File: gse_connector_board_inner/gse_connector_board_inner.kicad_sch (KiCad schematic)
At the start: 26 parts, among them J1 arming_connector, J2 gse_com_connector, J3 chg_connector, J4 Conn_02x03_Top_Bottom, J5 Conn_02x02_Top_Bottom, U7 ISO1044BD, U9 MCP2562-E-SN

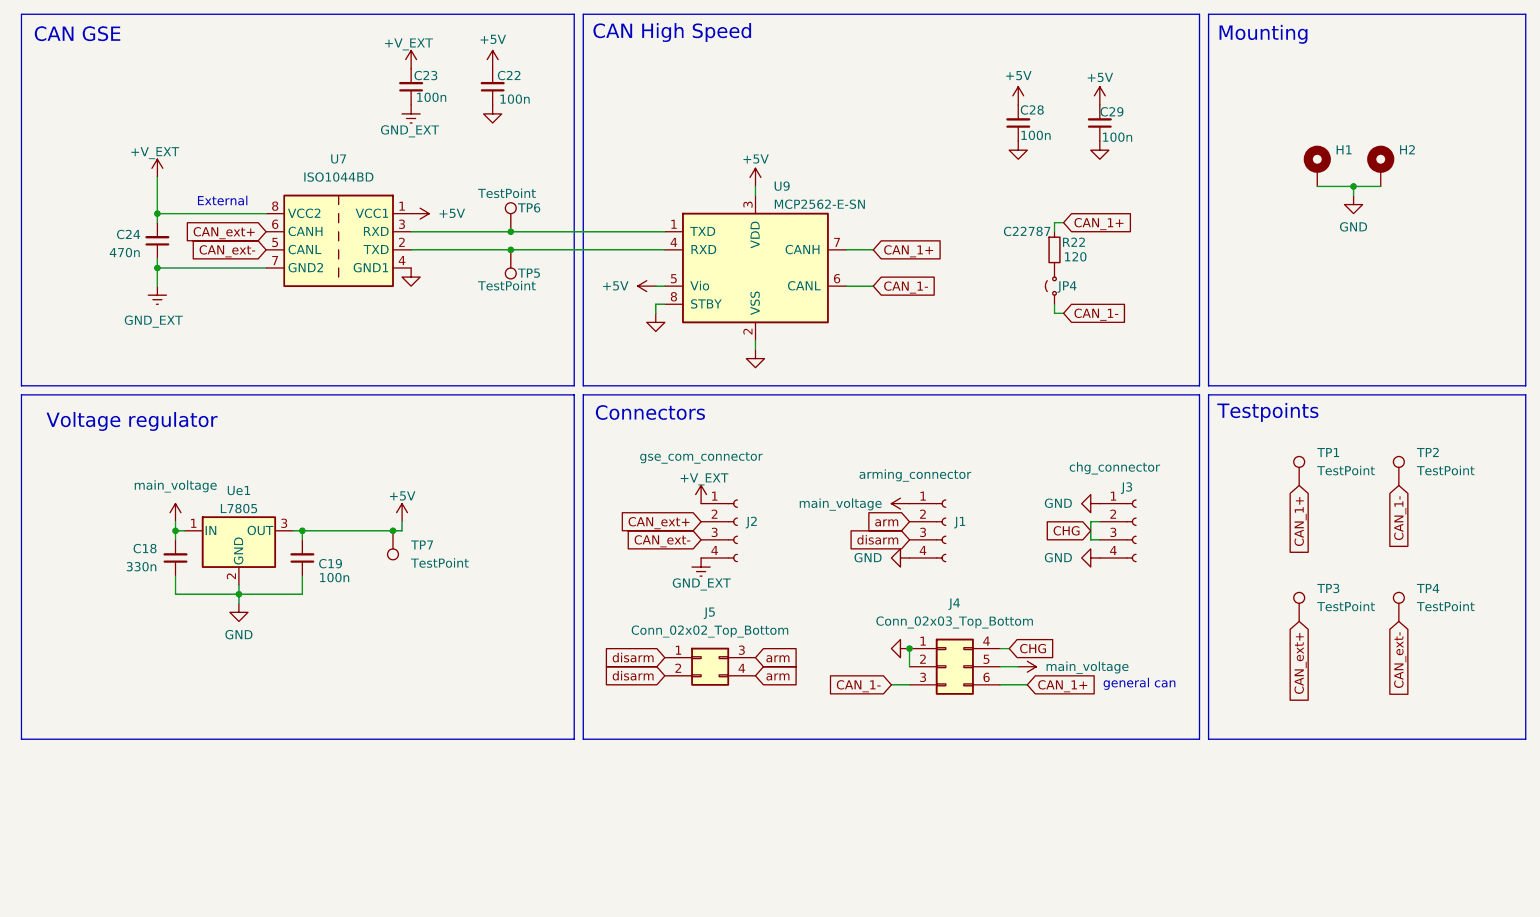
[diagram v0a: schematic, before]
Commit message: first draft of rev3 with new pogo pins
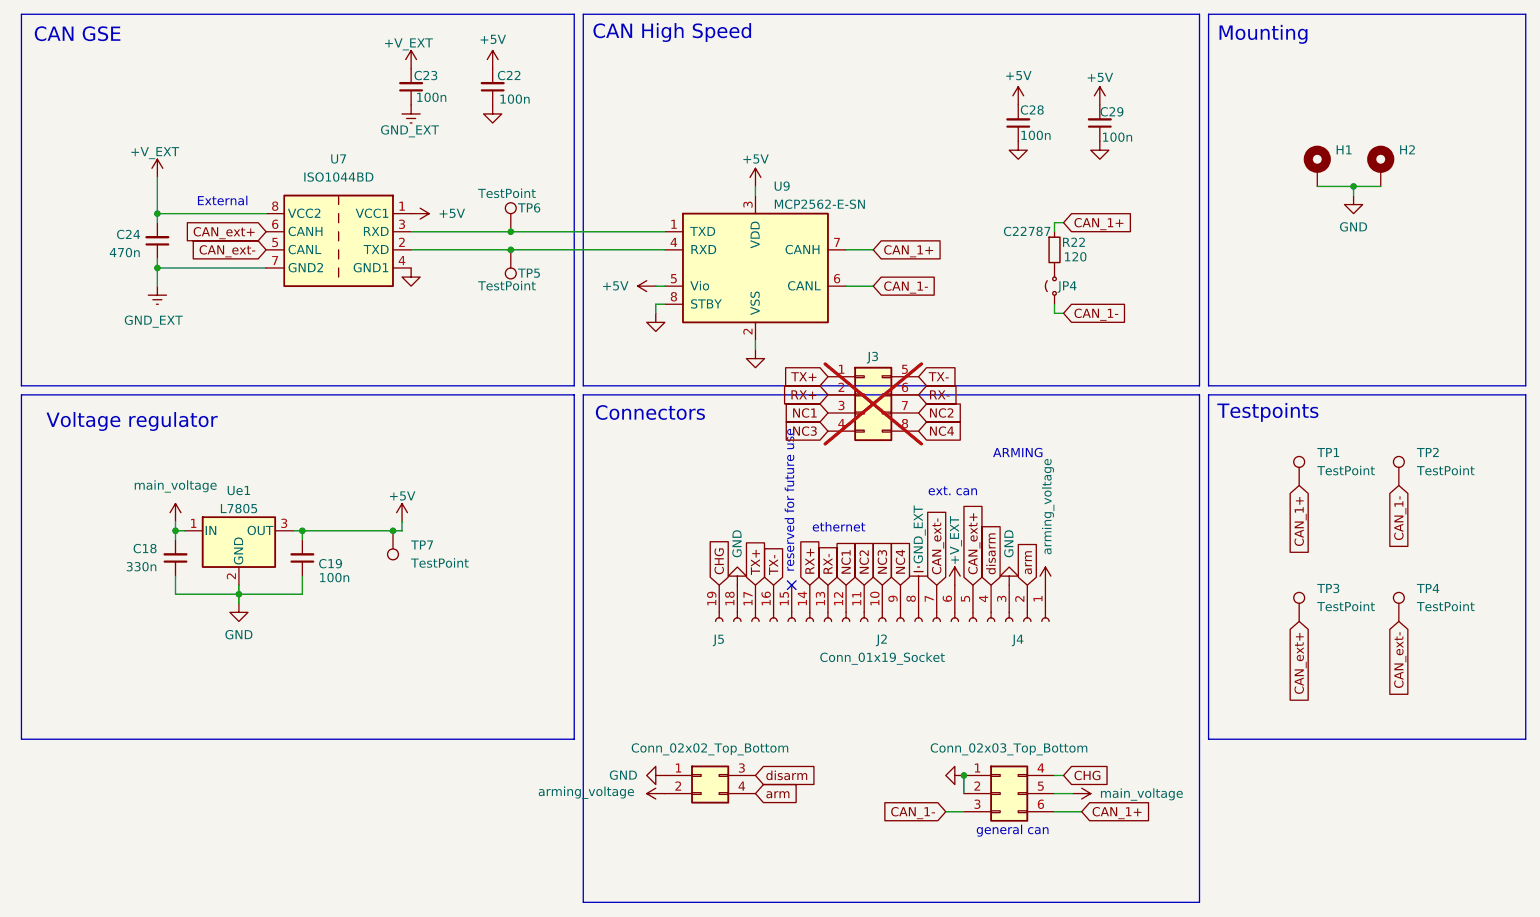
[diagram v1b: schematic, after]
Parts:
- removed J1: arming_connector, custom_parts:4_pin_mag_con_new, symbol Connector:Conn_01x04_Socket
- removed J2: gse_com_connector, custom_parts:4_pin_mag_con_new, symbol Connector:Conn_01x04_Socket
- removed J3: chg_connector, custom_parts:4_pin_mag_con_new, symbol Connector:Conn_01x04_Socket
- added J2: Conn_01x19_Socket, custom_parts:tudsat_gse_connector_rev_1, symbol Connector:Conn_01x19_Socket
- added J3: (no value), Connector_Molex:Molex_Micro-Fit_3.0_43045-0800_2x04_P3.00mm_Horizontal, symbol Connector_Generic:Conn_02x04_Top_Bottom
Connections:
- net +V_EXT: now also J2.6 (Pin_6)
- net CAN_ext+: now also J2.5 (Pin_5)
- net CAN_ext-: now also J2.7 (Pin_7)
- net CHG: now also J2.19 (Pin_19)
- net GND: now also J5.1 (Pin_1), J2.18 (Pin_18), J2.3 (Pin_3)
- net GND_EXT: now also J2.8 (Pin_8)
- net arm: now also J2.2 (Pin_2); no longer J5.3 (Pin_3)
- net disarm: now also J5.3 (Pin_3), J2.4 (Pin_4); no longer J5.1 (Pin_1), J5.2 (Pin_2)
- new net NC1: J2.12 (Pin_12), J3.3 (Pin_3)
- new net NC2: J2.11 (Pin_11), J3.7 (Pin_7)
- new net NC3: J2.10 (Pin_10), J3.4 (Pin_4)
- new net NC4: J2.9 (Pin_9), J3.8 (Pin_8)
- new net RX+: J2.14 (Pin_14), J3.2 (Pin_2)
- new net RX-: J2.13 (Pin_13), J3.6 (Pin_6)
- new net TX+: J2.17 (Pin_17), J3.1 (Pin_1)
- new net TX-: J2.16 (Pin_16), J3.5 (Pin_5)
- new net arming_voltage: J2.1 (Pin_1), J5.2 (Pin_2)
- no-connect marks 0 -> 1
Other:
- note added: "ARMING"
- note added: "ethernet"
- note added: "ext. can"
- note added: "reserved for future use"
- moved on the sheet: J4, J5
